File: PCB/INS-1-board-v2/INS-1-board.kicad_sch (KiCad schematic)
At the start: 11 parts, among them J1 Conn_3_screw_OSTVN03A150, Q1 MPSA42, Q2 MPSA42

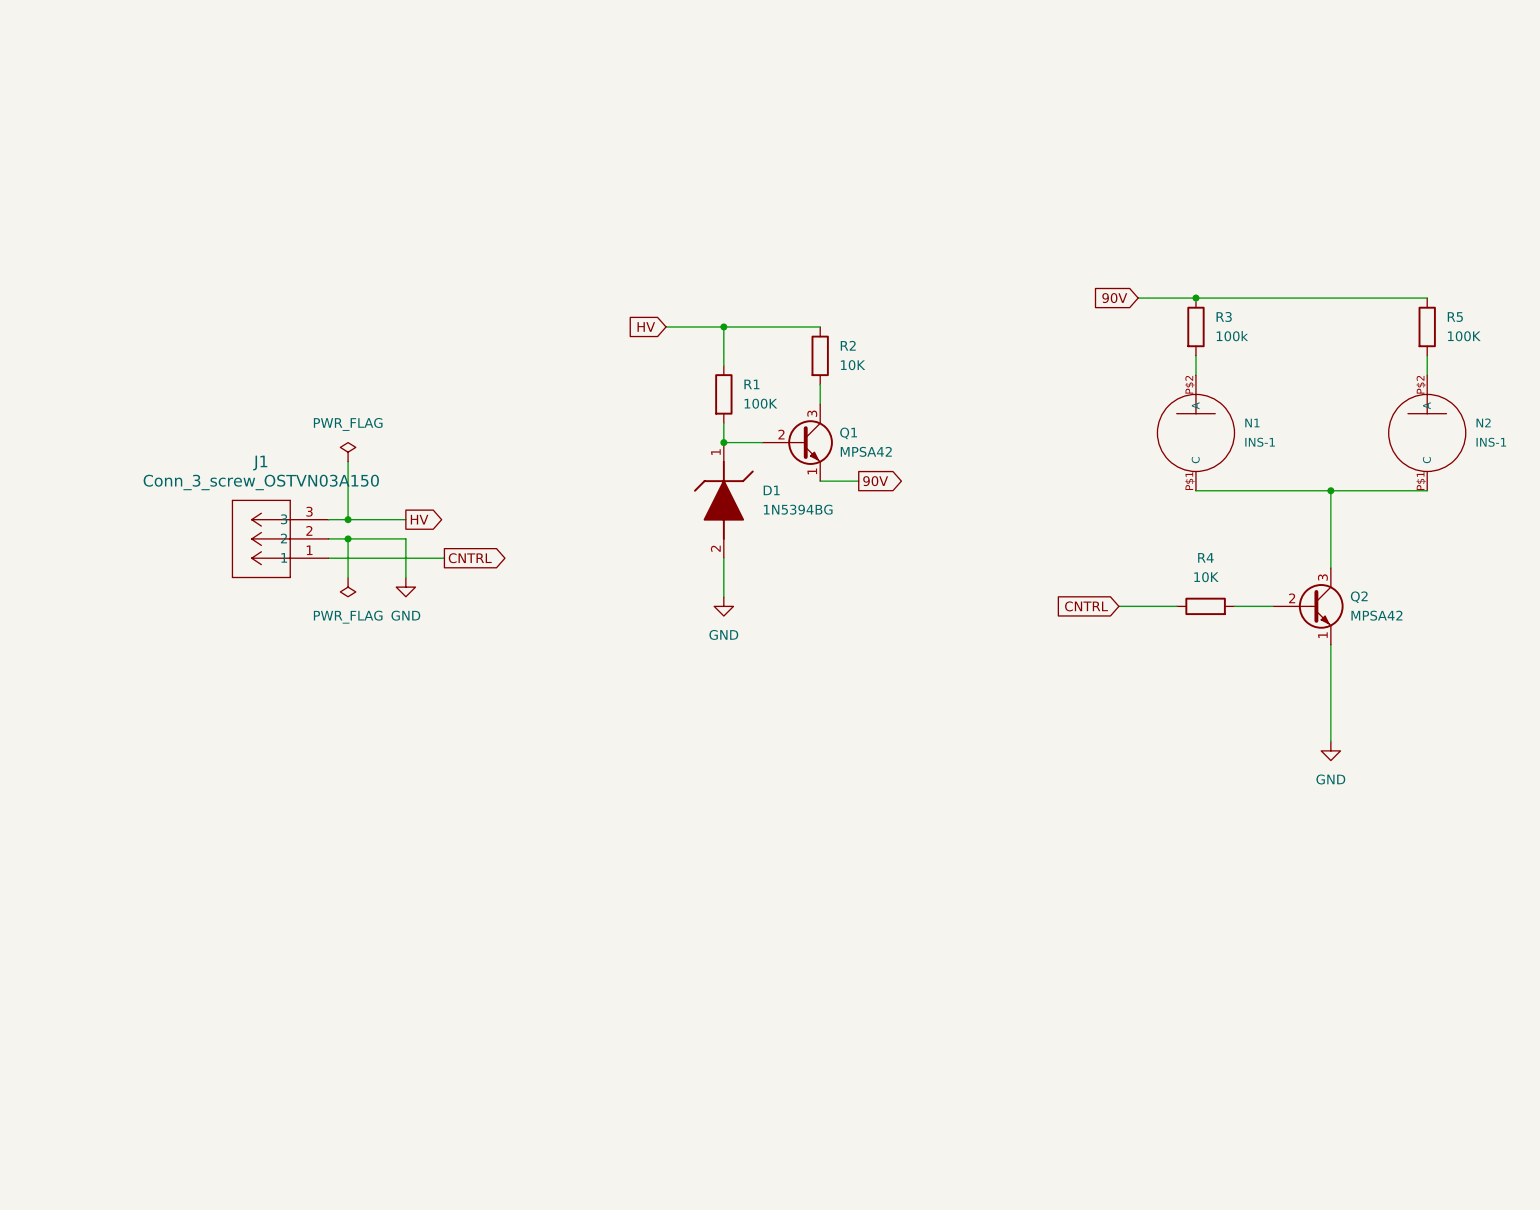
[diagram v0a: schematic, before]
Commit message: Moved docs to hv-ps-docs for the claude swe framework
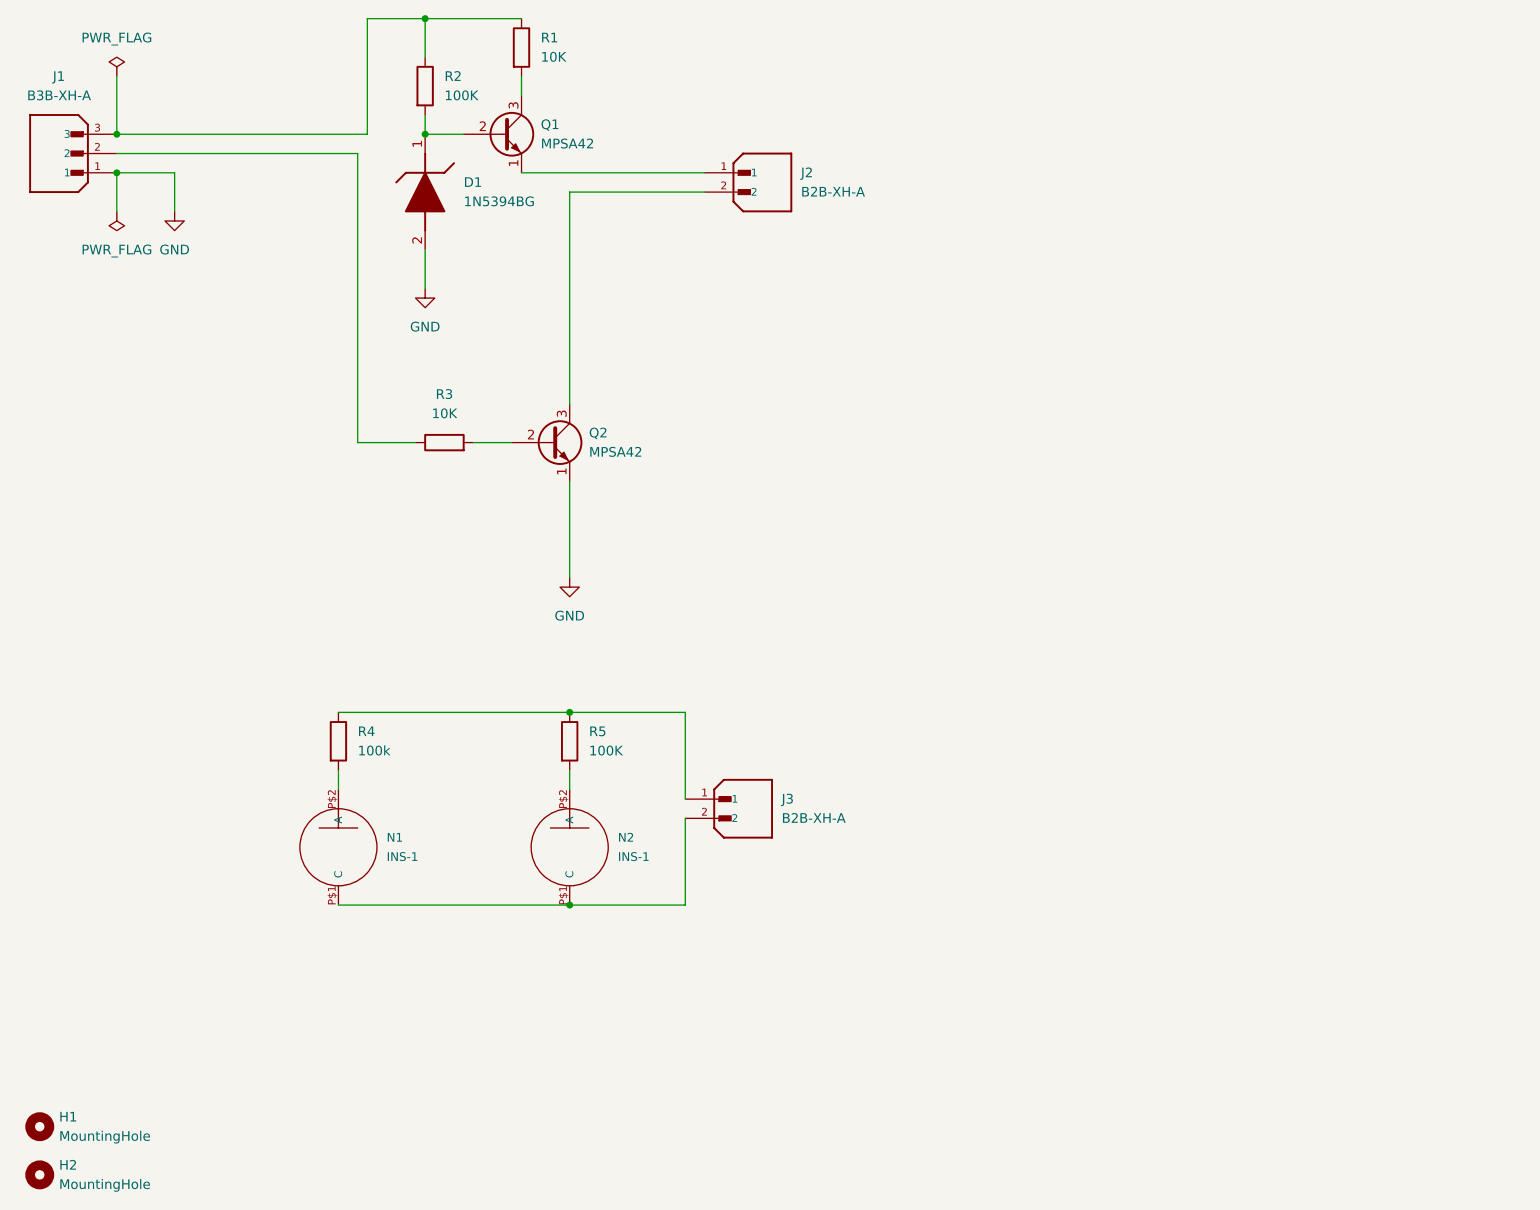
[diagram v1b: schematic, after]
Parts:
- removed J1: Conn_3_screw_OSTVN03A150, nixie-footprints:CONN3_OSTVN03A150_OST, symbol nixie-tube-clock-2.1:Conn_3_screw_OSTVN03A150
- added H1, H2: MountingHole, MountingHole:MountingHole_2.7mm, symbol Mechanical:MountingHole
- added J1: B3B-XH-A, INS-1-footprints:JST_B3B-XH-A, symbol INS-1-symbols:B3B-XH-A
- added J2, J3: B2B-XH-A, INS-1-footprints:JST_B2B-XH-A, symbol INS-1-symbols:B2B-XH-A
- D1: footprint DIOAD2260W109L864D349 -> INS-1-footprints:DIOAD2260W109L864D349
- Q1: footprint Package_TO_SOT_THT:TO-92_HandSolder -> INS-1-footprints:TO-92L_HandSolder
- R1: renamed from R2; footprint Resistor_THT:R_Axial_DIN0207_L6.3mm_D2.5mm_P7.62mm_Horizontal -> INS-1-footprints:R_Axial_DIN0207_L6.3mm_D2.5mm_P7.62mm_Horizontal
- R2: renamed from R1; footprint Resistor_THT:R_Axial_DIN0207_L6.3mm_D2.5mm_P7.62mm_Horizontal -> INS-1-footprints:R_Axial_DIN0207_L6.3mm_D2.5mm_P7.62mm_Horizontal
- R3: renamed from R4; footprint Resistor_THT:R_Axial_DIN0207_L6.3mm_D2.5mm_P7.62mm_Horizontal -> INS-1-footprints:R_Axial_DIN0207_L6.3mm_D2.5mm_P7.62mm_Horizontal
- R4: renamed from R3; footprint Resistor_THT:R_Axial_DIN0207_L6.3mm_D2.5mm_P7.62mm_Horizontal -> INS-1-footprints:R_Axial_DIN0207_L6.3mm_D2.5mm_P7.62mm_Horizontal
- R5: footprint Resistor_THT:R_Axial_DIN0207_L6.3mm_D2.5mm_P7.62mm_Horizontal -> INS-1-footprints:R_Axial_DIN0207_L6.3mm_D2.5mm_P7.62mm_Horizontal
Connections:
- net GND: now also J1.1
- net at N1.P$1 (C), N2.P$1 (C): now also J3.2; no longer Q2.3 (C)
- net 90V: no longer names the net of R4.1, R5.1
- net 90V: now also J3.1; no longer Q1.1 (E)
- net CNTRL: no longer names the net of R3.1
- net CNTRL: now also J1.2
- net HV: no longer names the net of R1.1, R2.1
- net HV: now also J1.3
- new net: J2.1, Q1.1 (E)
- new net: J2.2, Q2.3 (C)
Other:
- moved on the sheet: D1, N1, N2, Q1, Q2, R1, R2, R3, R4, R5
